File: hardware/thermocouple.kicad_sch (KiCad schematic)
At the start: 3 parts, among them U4 MAX6675

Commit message: finished layout
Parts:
- renumbered C10 to C9, R7 to R6, U4 to U3
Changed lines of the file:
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@@
   (symbol (lib_id "Device:R_Small") (at 137.16 107.95 0)
     (in_bom yes) (on_board yes)
-    (property "Reference" "R7" (id 0) (at 138.43 106.68 0)
+    (property "Reference" "R6" (id 0) (at 138.43 106.68 0)
       (effects (font (size 1.27 1.27)) (justify left))
     )
@@
   (symbol (lib_id "extraparts:MAX6675") (at 148.59 101.6 0)
     (in_bom yes) (on_board yes)
-    (property "Reference" "U4" (id 0) (at 142.24 91.44 0)
+    (property "Reference" "U3" (id 0) (at 142.24 91.44 0)
       (effects (font (size 1.27 1.27)) (justify left))
     )
@@
   (symbol (lib_id "Device:C_Small") (at 152.4 86.36 0)
     (in_bom yes) (on_board yes)
-    (property "Reference" "C10" (id 0) (at 154.94 85.09 0)
+    (property "Reference" "C9" (id 0) (at 154.94 85.09 0)
       (effects (font (size 1.27 1.27)) (justify left))
     )

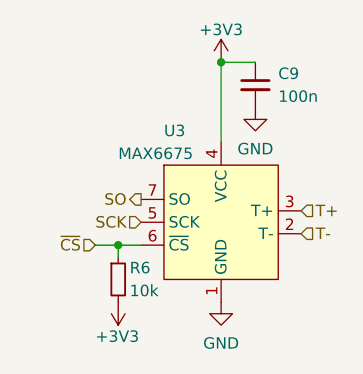
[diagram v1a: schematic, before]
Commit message: basic testing except heater done
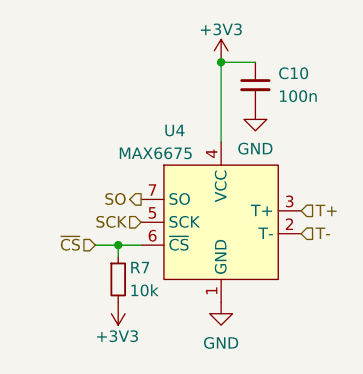
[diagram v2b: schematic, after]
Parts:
- renumbered C9 to C10, R6 to R7, U3 to U4
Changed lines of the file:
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@@
   (symbol (lib_id "Device:R_Small") (at 137.16 107.95 0)
     (in_bom yes) (on_board yes)
-    (property "Reference" "R6" (id 0) (at 138.43 106.68 0)
+    (property "Reference" "R7" (id 0) (at 138.43 106.68 0)
       (effects (font (size 1.27 1.27)) (justify left))
     )
@@
   (symbol (lib_id "extraparts:MAX6675") (at 148.59 101.6 0)
     (in_bom yes) (on_board yes)
-    (property "Reference" "U3" (id 0) (at 142.24 91.44 0)
+    (property "Reference" "U4" (id 0) (at 142.24 91.44 0)
       (effects (font (size 1.27 1.27)) (justify left))
     )
@@
   (symbol (lib_id "Device:C_Small") (at 152.4 86.36 0)
     (in_bom yes) (on_board yes)
-    (property "Reference" "C9" (id 0) (at 154.94 85.09 0)
+    (property "Reference" "C10" (id 0) (at 154.94 85.09 0)
       (effects (font (size 1.27 1.27)) (justify left))
     )
